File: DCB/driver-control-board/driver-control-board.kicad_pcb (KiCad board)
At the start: 2 copper layers, 95.5 x 61 mm, 32 parts, among them J1 Conn_01x05, J2 Conn_01x14, J3 Conn_01x08, J4 Conn_01x23, J5 Conn_02x10_Counter_Clockwise, J6 Conn_01x14, U1 STM32F413CGUx, U2 LD1117S33TR_SOT223, U3 R-78B5.0-2.0, U4 MCP2551-I-SN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

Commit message: Update layout with more connectors
Added passthrough for BMS
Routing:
- net +5V: track 38.0 -> 148.2 mm
- net +3V3: track 142.7 -> 159.4 mm, vias 6 -> 7
- net Net-(R7-Pad1): track 0.00 -> 7.10 mm
- net GND: vias 0 -> 14
- net (no net): vias 4 -> 0
- added copper zone on B.Cu, net GND
- added copper zone on F.Cu, net GND
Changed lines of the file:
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@@
     (property "Sheetname" "")
     (attr through_hole)
-    (fp_text reference "J4" (at -138.95 0.73702) (layer "F.SilkS")
+    (fp_text reference "J4" (at -13.462 6.35) (layer "F.SilkS")
       (effects (font (size 1.4012 1.4012) (thickness 0.05)))
     )
-    (fp_text value "Conn_01x23" (at -138.0689 21.5674) (layer "F.SilkS")
+    (fp_text value "Conn_01x23" (at -8.89 -0.762) (layer "F.SilkS")
       (effects (font (size 1.40221 1.40221) (thickness 0.05)))
     )
@@
   )
   (gr_rect (start 63.5 137.16) (end 159.004 76.2) (layer "Edge.Cuts") (width 0.1) (fill none))
-  (via (at 71.12 116.078) (size 0.8) (drill 0.4) (layers "F.Cu" "B.Cu") (free) (net 0))
-  (via (at 71.12 112.522) (size 0.8) (drill 0.4) (layers "F.Cu" "B.Cu") (free) (net 0))
-  (via (at 71.12 114.3) (size 0.8) (drill 0.4) (layers "F.Cu" "B.Cu") (free) (net 0))
-  (via (at 82.7786 110.4138) (size 0.8) (drill 0.4) (layers "F.Cu" "B.Cu") (free) (net 0))
-  (segment (start 81.244 103.16) (end 78.994 105.41) (width 0.254) (layer "F.Cu") (net 1))
-  (segment (start 76.744 107.66) (end 78.994 105.41) (width 0.254) (layer "F.Cu") (net 1))
+  (segment (start 76.962 107.442) (end 78.994 105.41) (width 0.254) (layer "F.Cu") (net 1))
+  (segment (start 81.244 103.16) (end 81.026 103.378) (width 0.254) (layer "F.Cu") (net 1))
+  (segment (start 76.744 107.66) (end 76.962 107.442) (width 0.254) (layer "F.Cu") (net 1))
   (segment (start 81.244 108.8475) (end 81.244 107.66) (width 0.254) (layer "F.Cu") (net 1))
   (segment (start 82.4315 104.66) (end 79.744 104.66) (width 0.254) (layer "F.Cu") (net 1))
   (segment (start 82.4315 103.16) (end 81.244 103.16) (width 0.254) (layer "F.Cu") (net 1))
+  (segment (start 81.026 107.442) (end 78.994 105.41) (width 0.254) (layer "F.Cu") (net 1))
+  (segment (start 81.026 103.378) (end 78.994 105.41) (width 0.254) (layer "F.Cu") (net 1))
   (segment (start 79.744 104.66) (end 78.994 105.41) (width 0.254) (layer "F.Cu") (net 1))
   (segment (start 75.5565 107.66) (end 76.744 107.66) (width 0.254) (layer "F.Cu") (net 1))
-  (segment (start 81.244 107.66) (end 78.994 105.41) (width 0.254) (layer "F.Cu") (net 1))
+  (segment (start 81.244 107.66) (end 81.026 107.442) (width 0.254) (layer "F.Cu") (net 1))
+  (via (at 81.026 103.378) (size 0.8) (drill 0.4) (layers "F.Cu" "B.Cu") (net 1))
+  (via (at 76.962 107.442) (size 0.8) (drill 0.4) (layers "F.Cu" "B.Cu") (net 1))
+  (via (at 121.92 83.82) (size 0.8) (drill 0.4) (layers "F.Cu" "B.Cu") (free) (net 1))
+  (via (at 76.962 103.378) (size 0.8) (drill 0.4) (layers "F.Cu" "B.Cu") (net 1))
+  (via (at 90.932 104.902) (size 0.8) (drill 0.4) (layers "F.Cu" "B.Cu") (free) (net 1))
+  (via (at 82.042 98.298) (size 0.8) (drill 0.4) (layers "F.Cu" "B.Cu") (free) (net 1))
+  (via (at 81.026 107.442) (size 0.8) (drill 0.4) (layers "F.Cu" "B.Cu") (net 1))
+  (via (at 71.374 116.078) (size 0.8) (drill 0.4) (layers "F.Cu" "B.Cu") (free) (net 1))
+  (via (at 71.374 114.554) (size 0.8) (drill 0.4) (layers "F.Cu" "B.Cu") (free) (net 1))
+  (via (at 87.884 108.966) (size 0.8) (drill 0.4) (layers "F.Cu" "B.Cu") (free) (net 1))
+  (via (at 90.932 103.378) (size 0.8) (drill 0.4) (layers "F.Cu" "B.Cu") (free) (net 1))
+  (via (at 121.92 81.28) (size 0.8) (drill 0.4) (layers "F.Cu" "B.Cu") (free) (net 1))
+  (via (at 71.374 113.03) (size 0.8) (drill 0.4) (layers "F.Cu" "B.Cu") (free) (net 1))
+  (via (at 121.92 86.36) (size 0.8) (drill 0.4) (layers "F.Cu" "B.Cu") (free) (net 1))
   (segment (start 74.676 117.19496) (end 74.80896 117.062) (width 0.36) (layer "F.Cu") (net 2))
   (segment (start 88.1888 95.504) (end 88.1888 96.8267) (width 0.36) (layer "F.Cu") (net 2))
@@
   (segment (start 85.20602 102.65348) (end 82.4315 102.65348) (width 0.36) (layer "F.Cu") (net 2))
   (segment (start 74.80896 111.28446) (end 73.7605 110.236) (width 0.36) (layer "F.Cu") (net 2))
+  (segment (start 98.044 118.618) (end 99.187 117.475) (width 0.36) (layer "F.Cu") (net 2))
   (segment (start 114.554 113.284) (end 125.628 113.284) (width 2.4) (layer "F.Cu") (net 2))
   (segment (start 131.928 113.284) (end 125.73 113.284) (width 1.2) (layer "F.Cu") (net 2))
@@
   (segment (start 84.328 109.5745) (end 84.2275 109.474) (width 0.36) (layer "F.Cu") (net 2))
   (segment (start 75.5565 108.16) (end 75.5565 108.44) (width 0.254) (layer "F.Cu") (net 2))
+  (segment (start 99.187 117.475) (end 100.649 117.475) (width 0.36) (layer "F.Cu") (net 2))
   (segment (start 113.013 108.886) (end 113.013 111.743) (width 2.4) (layer "F.Cu") (net 2))
   (segment (start 84.2275 109.474) (end 84.2275 110.6435) (width 0.36) (layer "F.Cu") (net 2))
   (segment (start 125.73 113.284) (end 125.628 113.284) (width 1.2) (layer "F.Cu") (net 2))
+  (segment (start 98.044 120.396) (end 100.2295 120.396) (width 0.36) (layer "F.Cu") (net 2))
   (segment (start 113.013 111.743) (end 114.554 113.284) (width 2.4) (layer "F.Cu") (net 2))
   (segment (start 85.2678 101.5238) (end 85.2678 102.5917) (width 0.36) (layer "F.Cu") (net 2))
@@
   (segment (start 88.1888 96.8267) (end 88.138 96.8775) (width 0.36) (layer "F.Cu") (net 2))
   (segment (start 84.2275 110.6435) (end 84.328 110.744) (width 0.36) (layer "F.Cu") (net 2))
+  (segment (start 98.044 120.396) (end 98.044 118.618) (width 0.36) (layer "F.Cu") (net 2))
   (segment (start 123.0365 108.9785) (end 123.049 108.966) (width 0.36) (layer "F.Cu") (net 2))
   (segment (start 73.7605 110.236) (end 73.7605 109.675) (width 0.254) (layer "F.Cu") (net 2))
   (via (at 74.676 119.38) (size 0.8) (drill 0.4) (layers "F.Cu" "B.Cu") (net 2))
   (via (at 88.1888 95.504) (size 0.8) (drill 0.4) (layers "F.Cu" "B.Cu") (net 2))
+  (via (at 98.044 120.396) (size 0.8) (drill 0.4) (layers "F.Cu" "B.Cu") (net 2))
   (via (at 85.2678 101.5238) (size 0.8) (drill 0.4) (layers "F.Cu" "B.Cu") (net 2))
   (via (at 125.73 111.76) (size 0.8) (drill 0.4) (layers "F.Cu" "B.Cu") (net 2))
@@
   (segment (start 84.328 111.506) (end 84.328 110.744) (width 0.36) (layer "B.Cu") (net 2))
   (segment (start 85.2678 101.5238) (end 88.1888 98.6028) (width 0.36) (layer "B.Cu") (net 2))
+  (segment (start 99.314 121.666) (end 98.044 120.396) (width 0.36) (layer "B.Cu") (net 2))
+  (segment (start 107.188 121.666) (end 89.662 121.666) (width 0.36) (layer "B.Cu") (net 2))
   (segment (start 88.1888 98.6028) (end 88.1888 95.504) (width 0.36) (layer "B.Cu") (net 2))
   (segment (start 84.328 116.332) (end 84.328 111.506) (width 0.36) (layer "B.Cu") (net 2))
+  (segment (start 122.936 121.666) (end 107.188 121.666) (width 0.36) (layer "B.Cu") (net 2))
   (segment (start 89.662 121.666) (end 76.962 121.666) (width 0.36) (layer "B.Cu") (net 2))
   (segment (start 125.73 118.872) (end 122.936 121.666) (width 0.36) (layer "B.Cu") (net 2))
   (segment (start 84.328 102.4636) (end 85.2678 101.5238) (width 0.36) (layer "B.Cu") (net 2))
-  (segment (start 122.936 121.666) (end 89.662 121.666) (width 0.36) (layer "B.Cu") (net 2))
+  (segment (start 107.188 121.666) (end 99.314 121.666) (width 0.36) (layer "B.Cu") (net 2))
   (segment (start 79.244 101.9725) (end 79.244 100.842) (width 0.254) (layer "F.Cu") (net 3))
   (segment (start 79.756 100.33) (end 98.43 100.33) (width 0.254) (layer "F.Cu") (net 3))
@@
   (segment (start 88.135 98.7025) (end 86.36 96.9275) (width 0.254) (layer "F.Cu") (net 7))
   (segment (start 123.480688 95.4615) (end 109.427188 81.408) (width 2.4) (layer "F.Cu") (net 8))
+  (segment (start 68.58 77.724) (end 65.267479 81.036521) (width 1.2) (layer "F.Cu") (net 8))
   (segment (start 126.5705 95.4615) (end 123.480688 95.4615) (width 2.4) (layer "F.Cu") (net 8))
+  (segment (start 65.267479 81.036521) (end 65.267479 131.815479) (width 1.2) (layer "F.Cu") (net 8))
+  (segment (start 90.678 77.724) (end 68.58 77.724) (width 1.2) (layer "F.Cu") (net 8))
+  (segment (start 65.267479 131.815479) (end 68.58 135.128) (width 1.2) (layer "F.Cu") (net 8))
+  (segment (start 68.58 135.128) (end 86.93 135.128) (width 1.2) (layer "F.Cu") (net 8))
   (segment (start 109.427188 81.408) (end 94.362 81.408) (width 2.4) (layer "F.Cu") (net 8))
+  (segment (start 94.362 81.408) (end 90.678 77.724) (width 1.2) (layer "F.Cu") (net 8))
+  (segment (start 86.93 135.128) (end 90.042 132.016) (width 1.2) (layer "F.Cu") (net 8))
   (segment (start 121.299 107.4795) (end 121.2615 107.442) (width 0.36) (layer "F.Cu") (net 9))
   (segment (start 121.299 107.4045) (end 121.2615 107.442) (width 0.36) (layer "F.Cu") (net 9))
@@
   (segment (start 88.915311 101.559289) (end 88.915311 95.203068) (width 0.254) (layer "B.Cu") (net 34))
   (segment (start 88.915311 95.203068) (end 90.362 93.756379) (width 0.254) (layer "B.Cu") (net 34))
+  (segment (start 103.886 120.0385) (end 103.886 115.316) (width 0.254) (layer "F.Cu") (net 35))
+  (segment (start 103.886 115.316) (end 104.267 114.935) (width 0.254) (layer "F.Cu") (net 35))
+  (segment (start 104.2435 120.396) (end 103.886 120.0385) (width 0.254) (layer "F.Cu") (net 35))
+  (segment (start 104.267 114.935) (end 105.599 114.935) (width 0.254) (layer "F.Cu") (net 35))
   (segment (start 75.5565 107.16) (end 74.5505 107.16) (width 0.254) (layer "F.Cu") (net 41))
   (segment (start 74.5505 107.16) (end 73.7605 107.95) (width 0.254) (layer "F.Cu") (net 41))
@@
   (segment (start 138.4885 114.5597) (end 134.97 118.0782) (width 0.2) (layer "F.Cu") (net 68))
   (segment (start 151.039001 104.370001) (end 141.820199 104.370001) (width 0.2) (layer "F.Cu") (net 68))
+  (zone (net 1) (net_name "GND") (layers F&B.Cu) (hatch edge 0.508)
+    (connect_pads (clearance 0.36))
+    (min_thickness 0.254) (filled_areas_thickness no)
+    (fill yes (thermal_gap 0.508) (thermal_bridge_width 0.508) (smoothing chamfer) (radius 1))
+    (polygon
+      (pts
+        (xy 157.48 134.62)
+        (xy 66.04 134.62)
+        (xy 66.04 78.74)
+        (xy 157.48 78.74)
+      )
+    )
+  )
 )

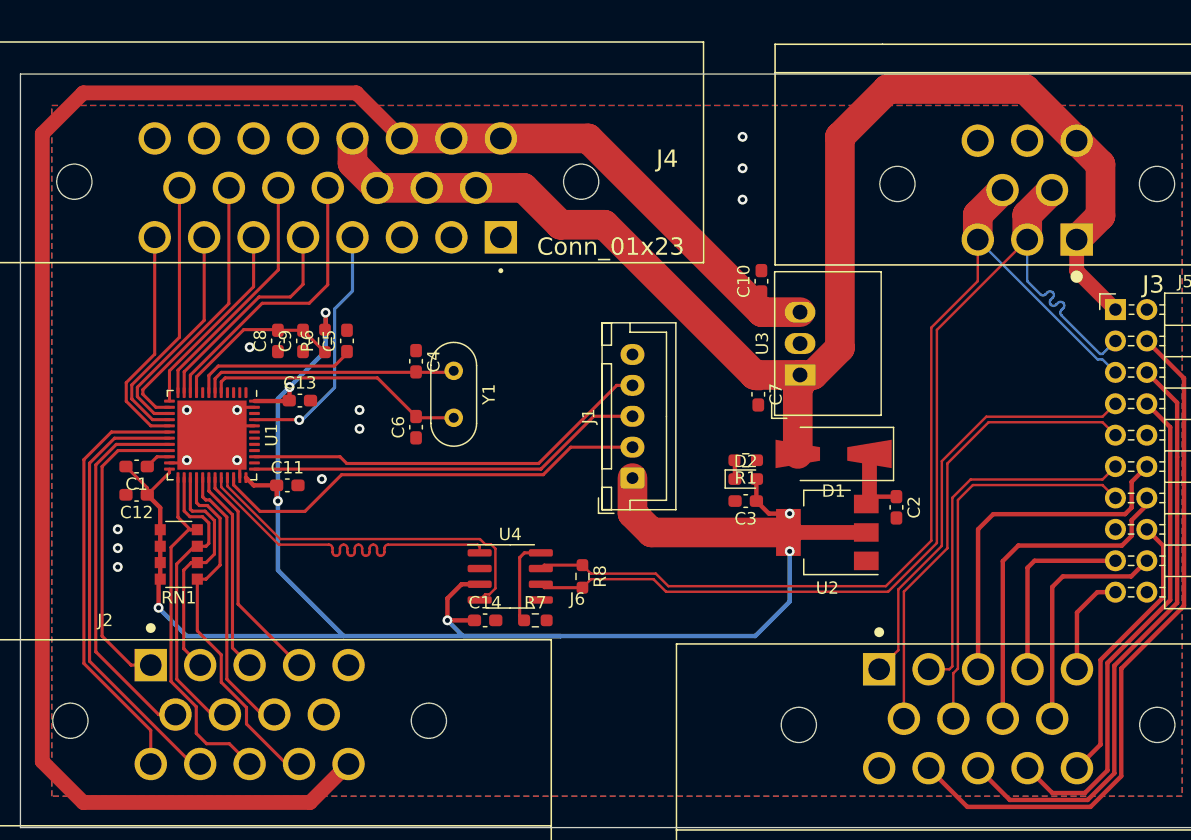
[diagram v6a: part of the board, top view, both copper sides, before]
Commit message: Major Review and Part Update
updating footprints, component values, layouts
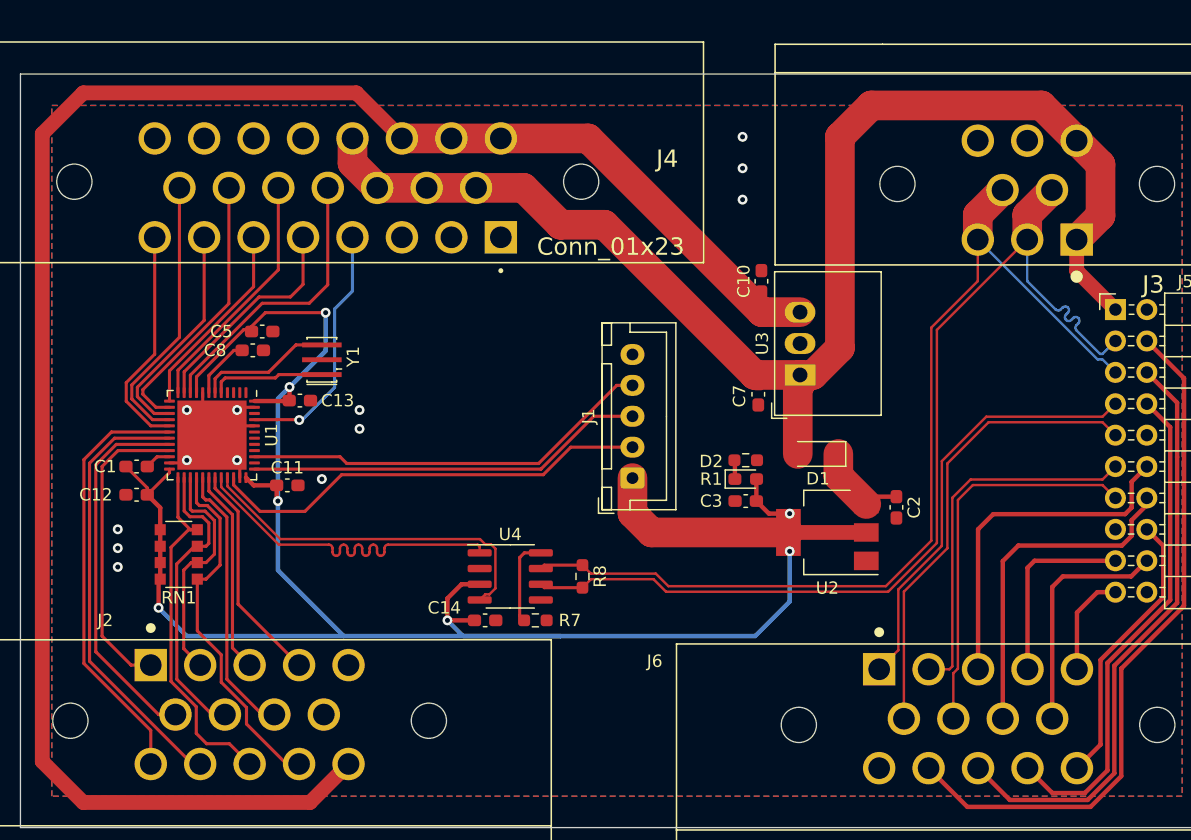
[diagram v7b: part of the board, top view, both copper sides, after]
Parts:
- removed C4, C6: 20p, Capacitor_SMD:C_0603_1608Metric_Pad1.08x0.95mm_HandSolder
- removed C9: 0.1u, Capacitor_SMD:C_0603_1608Metric_Pad1.08x0.95mm_HandSolder
- removed R6: R, Resistor_SMD:R_0603_1608Metric_Pad0.98x0.95mm_HandSolder
- D1: value D_Schottky -> BAT54gw; footprint Diode_SMD:D_SMA-SMB_Universal_Handsoldering -> Diode_SMD:D_SOD-123
- R1: value 220 -> 330
- Y1: value Crystal -> CSTNE8M00; footprint Crystal:Crystal_HC52-8mm_Vertical -> AERO_Footprints:Resonator_SMD_muRata_CSTxExxV-3Pin_3.0x1.1mm_HandSoldering
- moved Y1 10.7 mm to (87.9, 99.3), turned to 90 degrees
- moved C5 7.66 mm to (82.3, 98.6), turned to 0 degrees
- moved C8 1.48 mm to (83.1, 97.0), turned to 180 degrees
- moved D1 1.27 mm to (128.0, 106.9)
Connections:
- C8 pad 2: Net-(C8-Pad2) -> +3V3
- U1 pad 5: Net-(C6-Pad2) -> Net-(U1-Pad5)
- U1 pad 6: Net-(C4-Pad2) -> Net-(U1-Pad6)
- U1 pad 8: unconnected-(U1-Pad8) -> GND
- U1 pad 9: Net-(C8-Pad2) -> +3V3
- Y1 pad 1: Net-(C4-Pad2) -> Net-(U1-Pad5)
- Y1 pad 2: Net-(C6-Pad2) -> GND
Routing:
- net Net-(C6-Pad2): track 21.1 -> 0.00 mm
- net Net-(C4-Pad2): track 20.7 -> 0.00 mm
- net Net-(C8-Pad2): track 14.0 -> 0.00 mm
- net +3V3: track 159.4 -> 171.9 mm
- net Net-(U1-Pad6): track 0.00 -> 10.9 mm
- net Net-(U1-Pad5): track 0.00 -> 9.25 mm
- net Net-(C5-Pad1): track 13.5 -> 4.92 mm
- net GND: track 16.9 -> 20.6 mm, vias 14 -> 13
- net /START_BTN: track 30.3 -> 28.5 mm
- net +12V: track 112.0 -> 110.9 mm
- net Net-(C2-Pad1): track 6.84 -> 7.67 mm
- net /LCD_BTN: track 19.6 -> 18.9 mm

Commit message: updating schem and layout. WIP
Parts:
- removed C13, C14: 0.1u, Capacitor_SMD:C_0603_1608Metric_Pad1.08x0.95mm_HandSolder
- removed C2: .1u, Capacitor_SMD:C_0603_1608Metric_Pad1.08x0.95mm_HandSolder
- removed C3: 10u, Capacitor_SMD:C_0603_1608Metric_Pad1.08x0.95mm_HandSolder
- removed J1: Conn_01x05, Connector_JST:JST_XH_B5B-XH-A_1x05_P2.50mm_Vertical
- removed R7: 1k, Resistor_SMD:R_0603_1608Metric_Pad0.98x0.95mm_HandSolder
- removed R8: 120, Resistor_SMD:R_0603_1608Metric_Pad0.98x0.95mm_HandSolder
- removed U2: LD1117S33TR_SOT223, Package_TO_SOT_SMD:SOT-223-3_TabPin2
- added C4: 4.7u, Capacitor_SMD:C_0603_1608Metric_Pad1.08x0.95mm_HandSolder, F.Cu at (73.4, 111.8)
- added C6: 10u, Capacitor_SMD:C_0603_1608Metric_Pad1.08x0.95mm_HandSolder, F.Cu at (119.8, 104.1)
- added C9: 0.1u, Capacitor_SMD:C_0603_1608Metric_Pad1.08x0.95mm_HandSolder, B.Cu at (73.4, 113.5)
- added D3: SP0502BAHT, Package_TO_SOT_SMD:SOT-23, F.Cu at (75.0, 93.9)
- added D4: SP0502BAHT, Package_TO_SOT_SMD:SOT-23, F.Cu at (79.0, 93.9)
- added D5: SP0502BAHT, Package_TO_SOT_SMD:SOT-23, F.Cu at (83.1, 93.9)
- added D6: SP0502BAHT, Package_TO_SOT_SMD:SOT-23, F.Cu at (87.2, 93.9)
- added D9: DESD2CAN2SOQ-7, Package_TO_SOT_SMD:SOT-23, F.Cu at (100.6, 117.3)
- added J7: FTSH-107-01-F-DV-K, Connector_PinHeader_1.27mm:PinHeader_2x07_P1.27mm_Vertical_SMD, F.Cu at (97.5, 106.9)
- added JP1: SolderJumper_2_Bridged, Jumper:SolderJumper-2_P1.3mm_Bridged_Pad1.0x1.5mm, F.Cu at (87.6, 109.5)
- added Q1: 2N7002, Package_TO_SOT_SMD:SOT-23, F.Cu at (91.2, 93.9)
- added R10: 100, Resistor_SMD:R_0603_1608Metric_Pad0.98x0.95mm_HandSolder, F.Cu at (103.4, 105.7)
- added R2: 330, Resistor_SMD:R_0603_1608Metric_Pad0.98x0.95mm_HandSolder, F.Cu at (114.7, 106.6)
- added R6: 120, Resistor_SMD:R_0603_1608Metric_Pad0.98x0.95mm_HandSolder, F.Cu at (97.2, 117.2)
- C1: value 4.7u -> .1u
- C10: value 10u -> 0.1u
- C11, C5: moved to B.Cu
- C7: value .1u -> 0.1u; moved to B.Cu
- D1: value BAT54gw -> LED; footprint Diode_SMD:D_SOD-123 -> LED_SMD:LED_0603_1608Metric_Pad1.05x0.95mm_HandSolder
- D2: value LED -> SP0502BAHT; footprint LED_SMD:LED_0603_1608Metric_Pad1.05x0.95mm_HandSolder -> Package_TO_SOT_SMD:SOT-23
- R1: value 330 -> 10k
- U3: value R-78B5.0-2.0 -> LDL1117S33R; footprint Converter_DCDC:Converter_DCDC_RECOM_R-78B-2.0_THT -> Package_TO_SOT_SMD:SOT-223-3_TabPin2
- U4: value MCP2551-I-SN -> MAX33054EASA+T; footprint Package_SO:SOIC-8_3.9x4.9mm_P1.27mm -> AERO_Footprints:SOIC127P600X175-8N
- moved D2 54.2 mm to (68.1, 112.3), turned to 90 degrees
- moved C1 49.7 mm to (122.2, 101.8)
- moved C7 46.0 mm to (77.2, 103.4), turned to 180 degrees
- moved C10 40.8 mm to (84.8, 106.2), turned to -90 degrees
- moved R1 32.6 mm to (91.2, 97.3), turned to 0 degrees
- moved C8 25.9 mm to (93.3, 120.8), turned to 0 degrees
- moved C12 19.9 mm to (89.8, 120.8)
- moved D1 17.2 mm to (110.9, 104.9), turned to -90 degrees
- moved U4 11.6 mm to (91.5, 116.9)
- moved U3 11.0 mm to (115.6, 101.0)
- moved C11 6.14 mm to (83.2, 115.3), turned to 180 degrees
- moved C5 5.90 mm to (77.2, 101.6), turned to 180 degrees
- moved Y1 5.58 mm to (83.3, 102.5)
- moved U1 4.17 mm to (79.4, 109.6)
- moved RN1 4.12 mm to (73.5, 118.1), turned to -90 degrees
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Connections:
- C1 pad 1: Net-(C1-Pad1) -> +12V
- C1 pad 2: +3V3 -> GND
- C10 pad 1: +5V -> +3V3
- C7 pad 1: +12V -> +3V3
- C8 pad 1: GND -> +3V3
- C8 pad 2: +3V3 -> GND
- D1 pad 1: Net-(C2-Pad1) -> GND
- D1 pad 2: +12V -> Net-(D1-Pad2)
- D2 pad 1: Net-(D2-Pad1) -> /POT_REGEN
- D2 pad 2: +3V3 -> /POT_BRAKE
- J4 pad 10: +12V -> +3V3
- J4 pad 11: +12V -> +3V3
- J4 pad 16: +5V -> +3V3
- J4 pad 17: +5V -> +3V3
- J4 pad 18: +5V -> +3V3
- J4 pad 4: /RTD_IND -> /RTD_IND_OUT
- J4 pad 9: +12V -> +3V3
- R1 pad 1: GND -> /RTD_IND_SIG
- R1 pad 2: Net-(D2-Pad1) -> GND
- U1 pad 22: Net-(C1-Pad1) -> Net-(C4-Pad1)
- U1 pad 32: /CAN_X_P -> /CAN_RX
- U1 pad 33: /CAN_X_N -> /CAN_TX
- U1 pad 44: GND -> Net-(JP1-Pad2)
- U1 pad 45: /RTD_IND -> /RTD_IND_SIG
- U3 pad 1: +12V -> GND
- U3 pad 2: GND -> +3V3
- U3 pad 3: +5V -> +12V
- U4 pad 1: /CAN_X_P -> /CAN_TX
- U4 pad 4: /CAN_X_N -> /CAN_RX
- U4 pad 5: unconnected-(U4-Pad5) -> +3V3
- U4 pad 8: Net-(R7-Pad1) -> GND
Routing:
- net +3V3: track 171.9 -> 15.5 mm, vias 7 -> 3
- net +5V: track 148.2 -> 0.00 mm
- net +12V: track 110.9 -> 37.9 mm
- net /CAN_X_N: track 29.3 -> 0.00 mm
- net /CAN_X_P: track 29.1 -> 0.00 mm
- net /RTD_IND: track 20.3 -> 0.00 mm, vias 1 -> 0
- net B3_TRACESWO: track 33.4 -> 14.5 mm
- net A13_SWDIO: track 35.9 -> 17.3 mm
- net /RTD_IND_SIG: track 0.00 -> 18.1 mm
- net A14_SWCLK: track 32.4 -> 14.4 mm
- net /CAN_P: track 80.3 -> 93.3 mm
- net /CAN_RX: track 0.00 -> 12.0 mm
- net /CAN_TX: track 0.00 -> 11.9 mm
- net /CAN_N: track 82.4 -> 93.6 mm
- net Net-(C2-Pad1): track 7.67 -> 0.00 mm
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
